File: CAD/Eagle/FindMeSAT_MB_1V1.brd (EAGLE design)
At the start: 99 x 49.2 mm, 131 parts, among them J291 MCX-J-P-X-RA-SM1, J685 SMA_CON, J701 MOLEX_105017-0001, J801 MICROSIM-8P_SDCARD-8P_MOLEX-1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, J901 JST_S3B-XH-A, Q101 ABS07-32.768KHZ, Q651 ABM3B-16MHZ-10-R50-1-U, U1001 CFPT-141-20MHZ, U101 ATXMEGA256A3BU-AU, U1011 OPA354, U1021 OPA354, U1111 LM2831YMF, U1121 LM4120IM5-3.0, U201 SIM808, U301 MPU-9250, U401 MS5607-02BA03, U501 SHT31-DIS, U601 AX5243

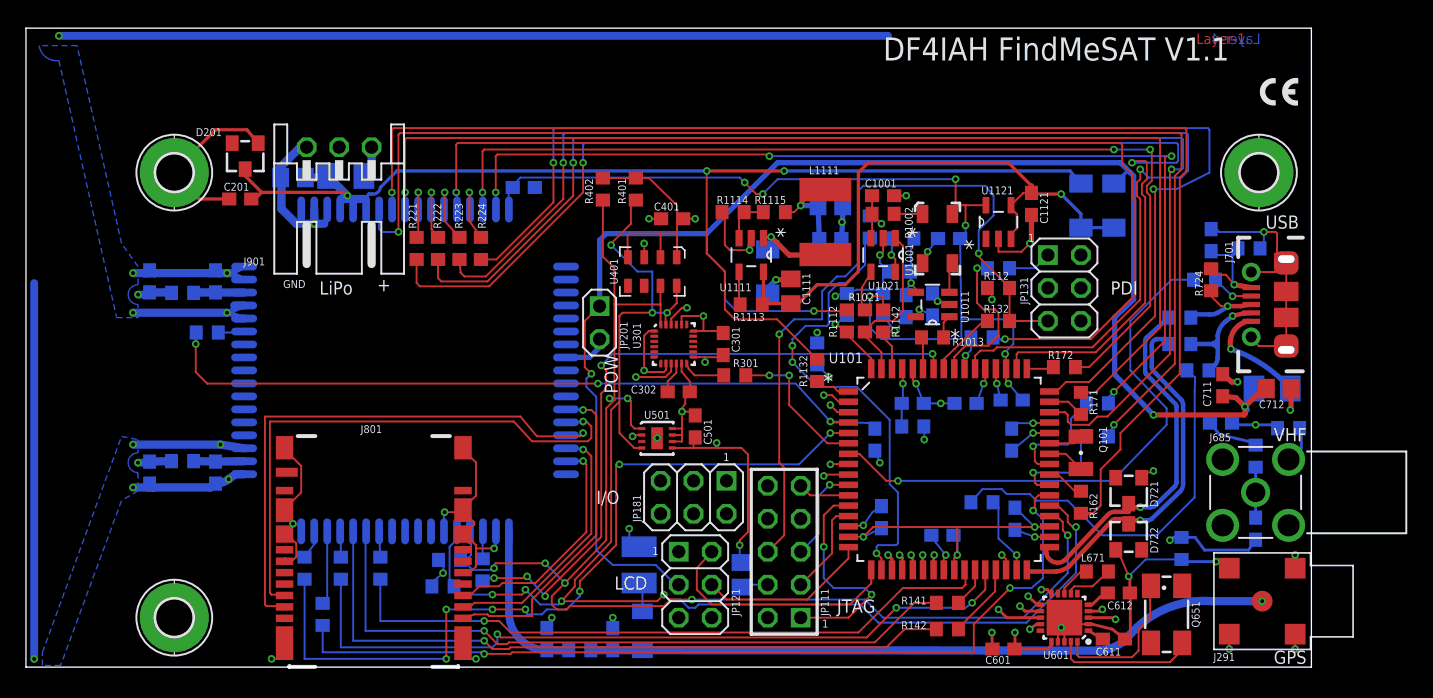
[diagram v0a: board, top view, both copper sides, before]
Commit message: CAD - multiple corrections of V1.1 redesign findings list
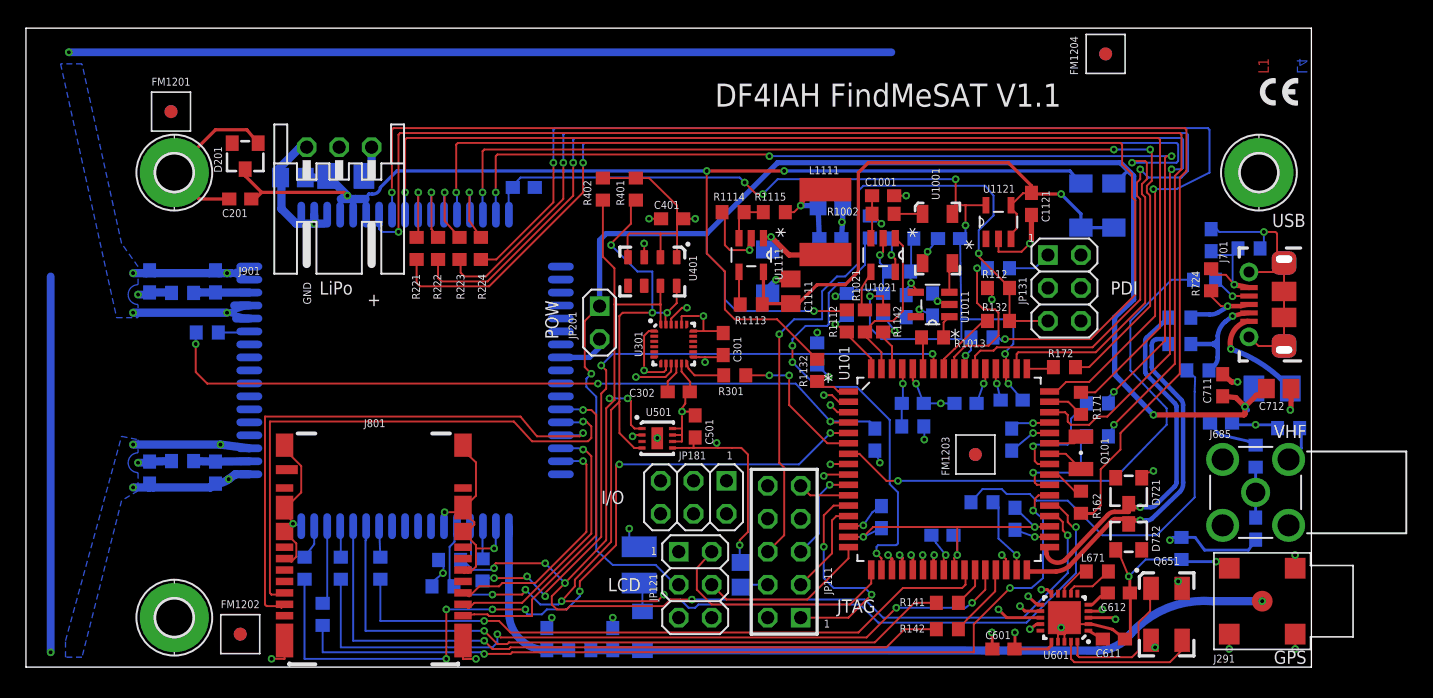
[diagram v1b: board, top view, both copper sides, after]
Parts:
- added FM1201, FM1202, FM1203, FM1204: FIDUCIAL_MARK_1MM, df4iah_fiducial:FIDUCIAL_MARK_1MM
- Q651: device adafruit:CTS406 -> df4iah_crystal:ABM03B
- moved U501 1.77 mm to (48.6, 17.6)
- moved J801 0.20 mm to (26.8, 9.09)
- moved J701 0.17 mm to (98.4, 27.9)
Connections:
- net +3V0: now also U201.17; no longer U201.P$17
- net BT_RF: now also U201.53; no longer U201.P$53
- net GND: now also Q651.2, Q651.4, U201.1, U201.18, U201.2, U201.28, U201.3, U201.34, U201.36, U201.40, U201.51, U201.52, U201.54, U201.64, U201.65, U201.67, U201.68; no longer U201.P$1, U201.P$18, U201.P$2, U201.P$28, U201.P$3, U201.P$34, U201.P$36, U201.P$40, U201.P$51, U201.P$52, U201.P$54, U201.P$64, U201.P$65, U201.P$67, U201.P$68
- net GPS_1PPS_DRV: now also U201.37; no longer U201.P$37
- net GPS_RF_IN: now also U201.35; no longer U201.P$35
- net GSM_CTS: now also U201.12; no longer U201.P$12
- net GSM_DCD: now also U201.11; no longer U201.P$11
- net GSM_DTR: now also U201.9; no longer U201.P$9
- net GSM_NETLIGHT_DRV: now also U201.50; no longer U201.P$50
- net GSM_PCM_CLK: now also U201.46; no longer U201.P$46
- net GSM_PCM_IN: now also U201.47; no longer U201.P$47
- net GSM_PCM_OUT_DRV: now also U201.48; no longer U201.P$48
- net GSM_PCM_SYNC_DRV: now also U201.45; no longer U201.P$45
- net GSM_PWRKEY: now also U201.8; no longer U201.P$8
- net GSM_RESET: now also U201.16; no longer U201.P$16
- net GSM_RF: now also U201.66; no longer U201.P$66
- net GSM_RF_SYNC_DRV: now also U201.63; no longer U201.P$63
- net GSM_RI: now also U201.10; no longer U201.P$10
- net GSM_RTS: now also U201.13; no longer U201.P$13
- net GSM_RXD: now also U201.15; no longer U201.P$15
- net GSM_STATUS_DRV: now also U201.49; no longer U201.P$49
- net GSM_TXD: now also U201.14; no longer U201.P$14
- net GSM_VDD_EXT: now also U201.7; no longer U201.P$7
- net SCL1: now also U201.39; no longer U201.P$39
- net SDA1: now also U201.38; no longer U201.P$38
- net SIM_CLK: now also U201.31; no longer U201.P$31
- net SIM_IO: now also U201.30; no longer U201.P$30
- net SIM_RST: now also U201.32; no longer U201.P$32
- net SIM_VBUS: now also U201.25; no longer U201.P$25
- net SIM_VCC: now also U201.29; no longer U201.P$29
- net SIM_VPP: now also U201.33; no longer U201.P$33
- net VBAT: now also U201.4, U201.5, U201.6; no longer U201.P$4, U201.P$5, U201.P$6
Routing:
- net GND: track 224.1 -> 227.4 mm, vias 52 -> 54
- net GSM_ANT: track 88.3 -> 86.3 mm
- net VBAT: track 95.6 -> 96.7 mm
- net BT_ANT: track 49.8 -> 48.8 mm
- net VIN: track 45.8 -> 46.6 mm
- net SIM_CLK: track 42.9 -> 43.4 mm
- added copper zone on layer 2, net N$1
- added copper zone on layer 2, net N$2
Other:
- board text added: "L1"
- board text added: "L2"
- board text added: "L3"
- board text added: "L4"
- board text removed: "Layer-1"
- board text removed: "Layer-2"
- board text removed: "Layer-3"
- board text removed: "Layer-4"

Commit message: CAD - work of the night
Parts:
- moved C501 3.09 mm to (54.6, 19.1), turned to 180 degrees
- moved JP181 1.83 mm to (49.9, 14.1)
- moved U501 1.02 mm to (48.6, 18.6)
- moved FM1201 0.89 mm to (11.2, 43.7)
- moved RPOLY291 0.89 mm to (46.4, 7.87)
- moved JP121 0.40 mm to (51.2, 6.48)
- moved JP111 0.13 mm to (58.4, 9.02)
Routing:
- net TCK: track 17.5 -> 10.7 mm
- net SDA2: track 13.2 -> 15.7 mm, vias 0 -> 1
- net IO_ADC4: track 25.2 -> 27.4 mm
- net GND: track 227.4 -> 229.1 mm
- net +3V3: track 100.3 -> 101.9 mm
- net IO_ADC5: track 17.9 -> 19.1 mm
- net GSM_DCD: track 5.38 -> 6.38 mm
- net SDA1: track 105.0 -> 104.1 mm
- net GPS_PWR: track 2.36 -> 3.25 mm
- net SCL2: track 19.0 -> 19.7 mm, vias 0 -> 1
- net GSM_PWRKEY: track 102.4 -> 103.1 mm
- net SCL1: track 110.7 -> 110.1 mm

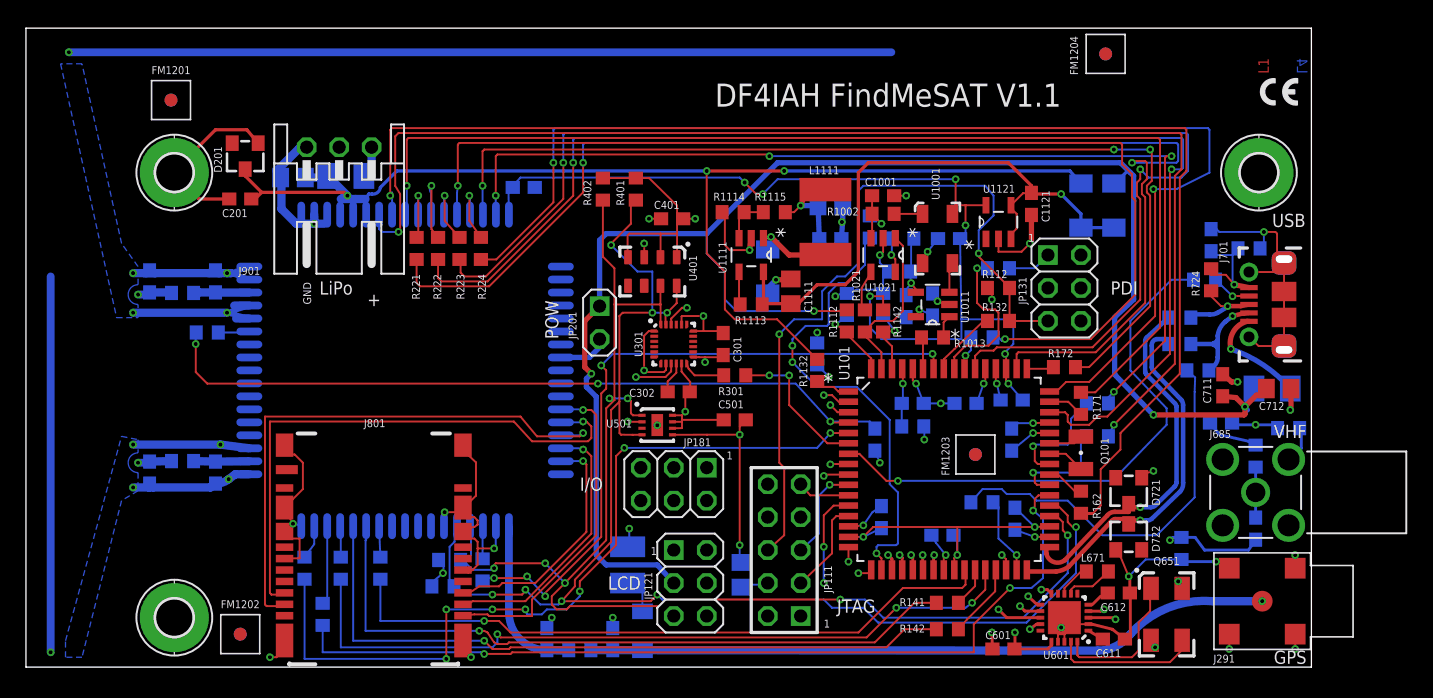
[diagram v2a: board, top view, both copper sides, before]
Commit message: CAD - first round of V1.0 --> V1.1 redesign done
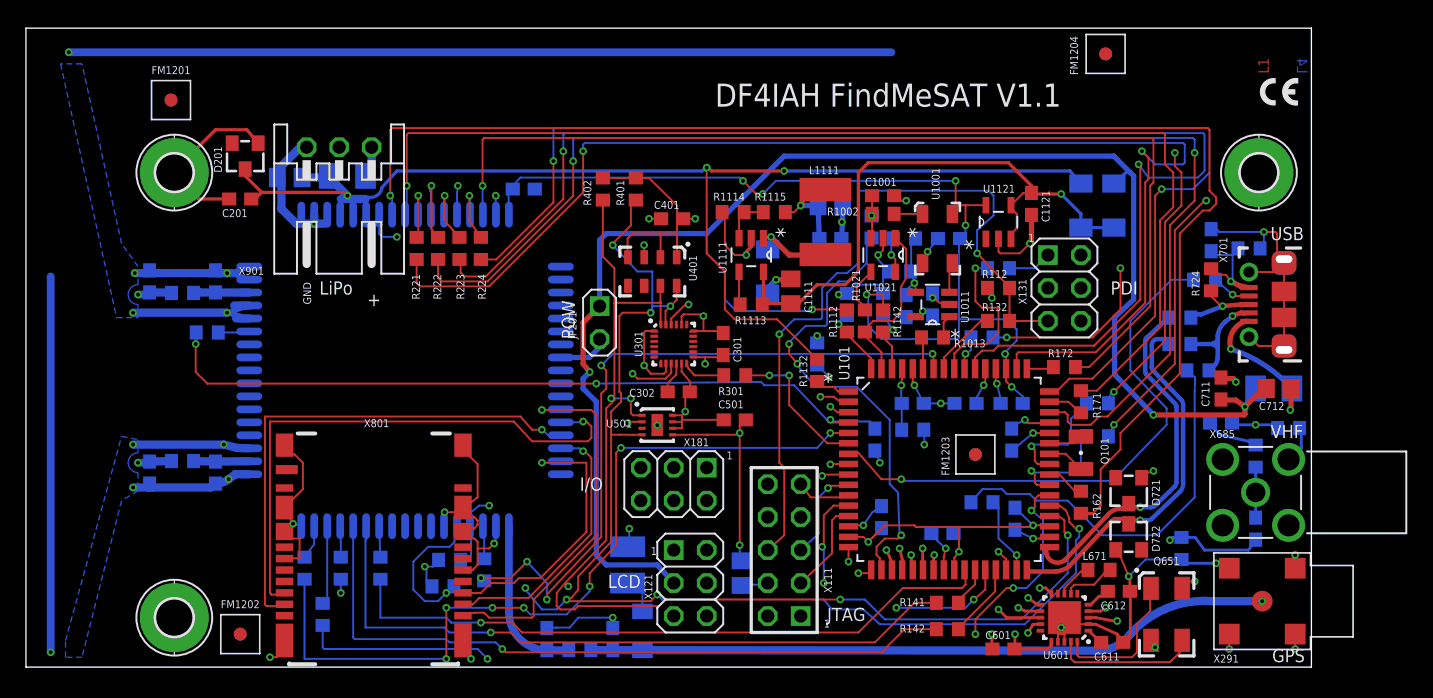
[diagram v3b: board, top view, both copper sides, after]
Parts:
- moved C611 0.28 mm to (83.7, 1.91)
- moved C711 0.28 mm to (92.1, 21.5)
- moved C101 0.25 mm to (75.9, 20.3)
- moved C901 0.25 mm to (20.3, 37.7)
- moved L191 0.25 mm to (68.3, 18.3)
- moved L671 0.18 mm to (82.7, 7.49)
- moved R1012 0.13 mm to (67.7, 33.0)
- moved C251 0.13 mm to (38.4, 36.8)
- moved C192 0.13 mm to (70.6, 10.3)
- moved C612 0.13 mm to (84.2, 5.84)
- moved R111 0.13 mm to (55.1, 7.24)
- moved R171 0.13 mm to (81.3, 20.4)
- moved RPOLY901 0.13 mm to (24.8, 37.8)
- moved R1001 0.13 mm to (65.2, 33.9)
- moved R251 0.13 mm to (35.3, 7.49)
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- renumbered J291 to X291, J685 to X685, J701 to X701, J801 to X801, J901 to X901, JP111 to X111, JP121 to X121, JP131 to X131, JP181 to X181
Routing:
- net GND: track 229.1 -> 236.9 mm, vias 54 -> 53
- net GSM_RTS: track 81.2 -> 88.5 mm, vias 2 -> 3
- net SCL1: track 110.1 -> 117.2 mm
- net GSM_VDD_EXT: track 96.5 -> 100.7 mm, vias 2 -> 3
- net SIM_CLK: track 43.3 -> 39.5 mm
- net SDA1: track 104.1 -> 107.4 mm, vias 7 -> 6
- net GSM_PWRKEY: track 103.1 -> 106.3 mm
- net SIM_VCC: track 25.8 -> 29.0 mm
- net GSM_RESET: track 78.0 -> 81.1 mm, vias 4 -> 3
- net RTS1: track 97.4 -> 100.5 mm
- net SIM_VPP: track 18.7 -> 21.7 mm
- net GPS_1PPS: track 53.2 -> 55.7 mm
- net GSM_DTR: track 86.6 -> 88.3 mm
- net GSM_RXD: track 76.5 -> 78.2 mm, vias 3 -> 1
- net XO_LP: track 5.51 -> 3.79 mm
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
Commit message: CAD/Docs - V1.1 candidate created
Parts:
- X111: value (none) -> AVR-JTAG-10; device df4iah_connector:AVR-JTAG-10 -> df4iah_connector:2X05
- X121: value (none) -> MOLEX_90130_2X03; device df4iah_connector:2X03 -> df4iah_connector:MOLEX_90130_2X03
- X131, X181: value (none) -> HEADER-2X3
- moved C501 0.89 mm to (53.7, 19.1)
- moved RPOLY291 0.76 mm to (45.6, 7.87)
- moved X121 0.63 mm to (50.5, 6.48)
- moved L291 0.38 mm to (47.1, 2.79)
- moved X181 0.25 mm to (49.9, 14.4)
- moved R111 0.13 mm to (55.0, 7.24)
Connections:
- net +3V3: now also X121.6; no longer X121.5
- net +5V: now also X121.4; no longer X121.3
- net GND: now also X121.2, X121.5; no longer X121.1, X121.6
- net SCL2: now also X121.1; no longer X121.2
- net SDA2: now also X121.3; no longer X121.4
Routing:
- net GND: track 236.9 -> 234.3 mm
- net GPS_ANT: track 54.8 -> 52.6 mm
- net SIM_IO: track 43.5 -> 42.1 mm
- net +3V3: track 101.2 -> 102.3 mm
- net IO_DAC0: track 16.3 -> 15.7 mm
- net SDA1: track 107.4 -> 108.0 mm
- net IO_DAC1: track 19.2 -> 18.7 mm

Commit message: CAD/Docs - V1.1 reworked to conform to PCB house Smart-Prototyping
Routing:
- net GND: track 234.3 -> 232.4 mm
- net CLK16P: track 11.2 -> 10.7 mm

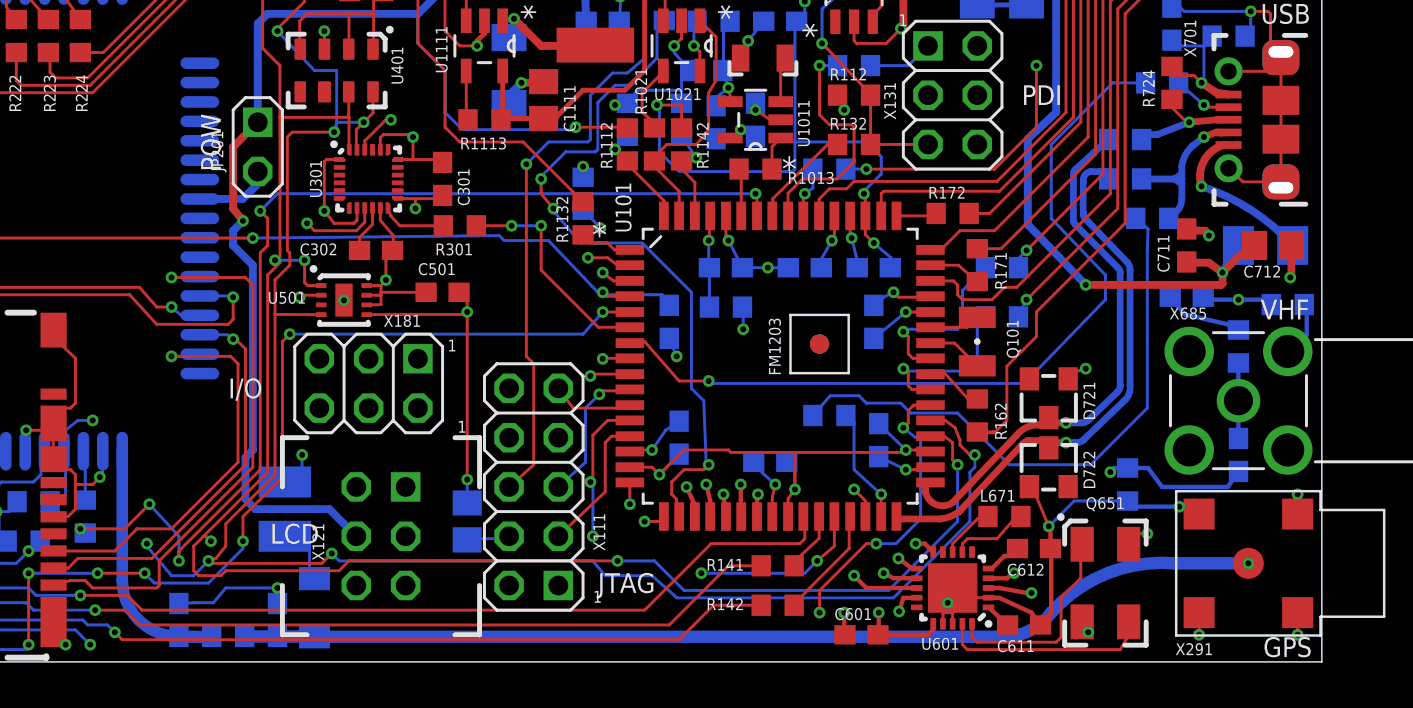
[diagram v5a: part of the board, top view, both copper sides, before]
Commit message: CAD - V1.1 impedance controlled lines corrected for reduced height of 0.120mm, gerber-inspection added
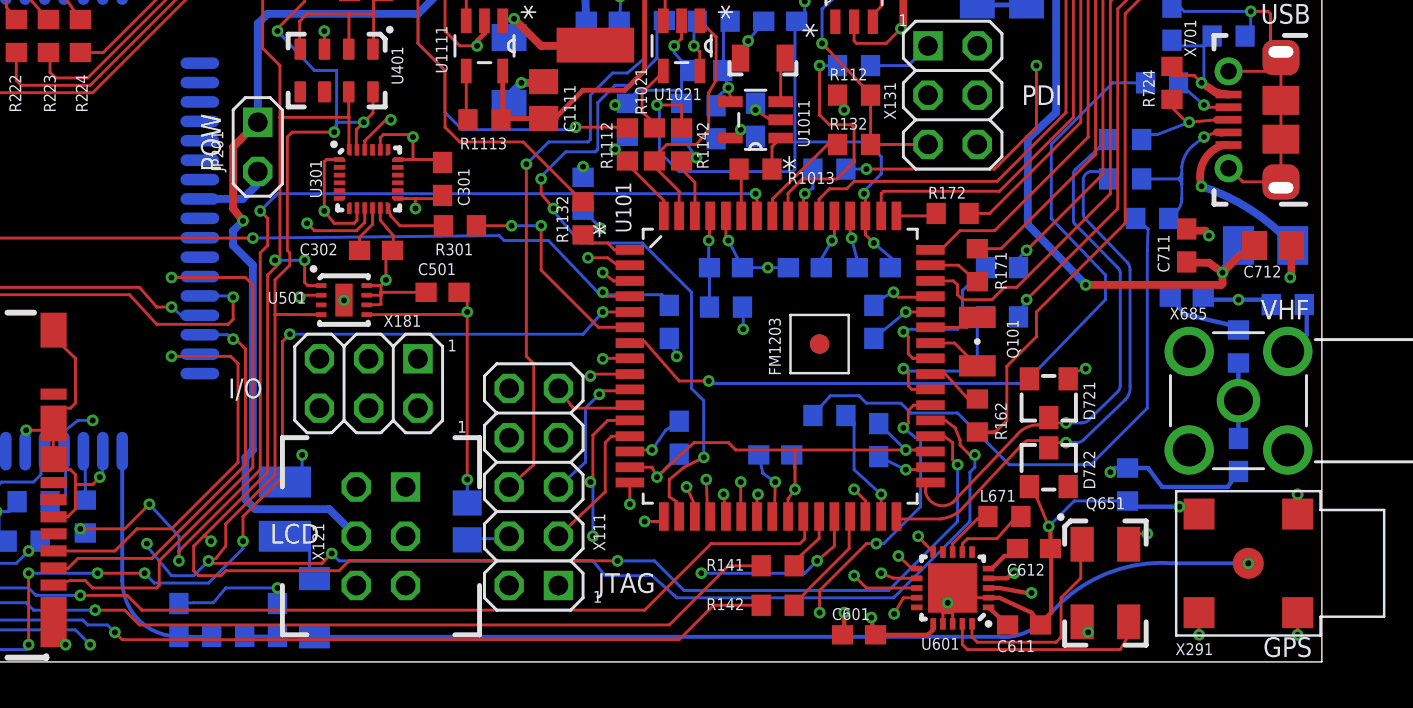
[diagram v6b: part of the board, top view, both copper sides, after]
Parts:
- moved C192 0.46 mm to (70.9, 10.7)
- moved C601 0.13 mm to (75.2, 1.40)
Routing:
- net +3V3: track 102.3 -> 103.0 mm
